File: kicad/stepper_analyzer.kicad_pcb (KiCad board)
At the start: 2 copper layers, 102 x 57 mm, 24 parts, among them J1 Connector_Conn_01x04_Male, J2 Connector_Conn_01x04_Male, M1 Motor, Q1 AO3400A, U1 ACS70331EOLCTR-2P5B3, U2 ACS70331EOLCTR-2P5B3, U3 Pico

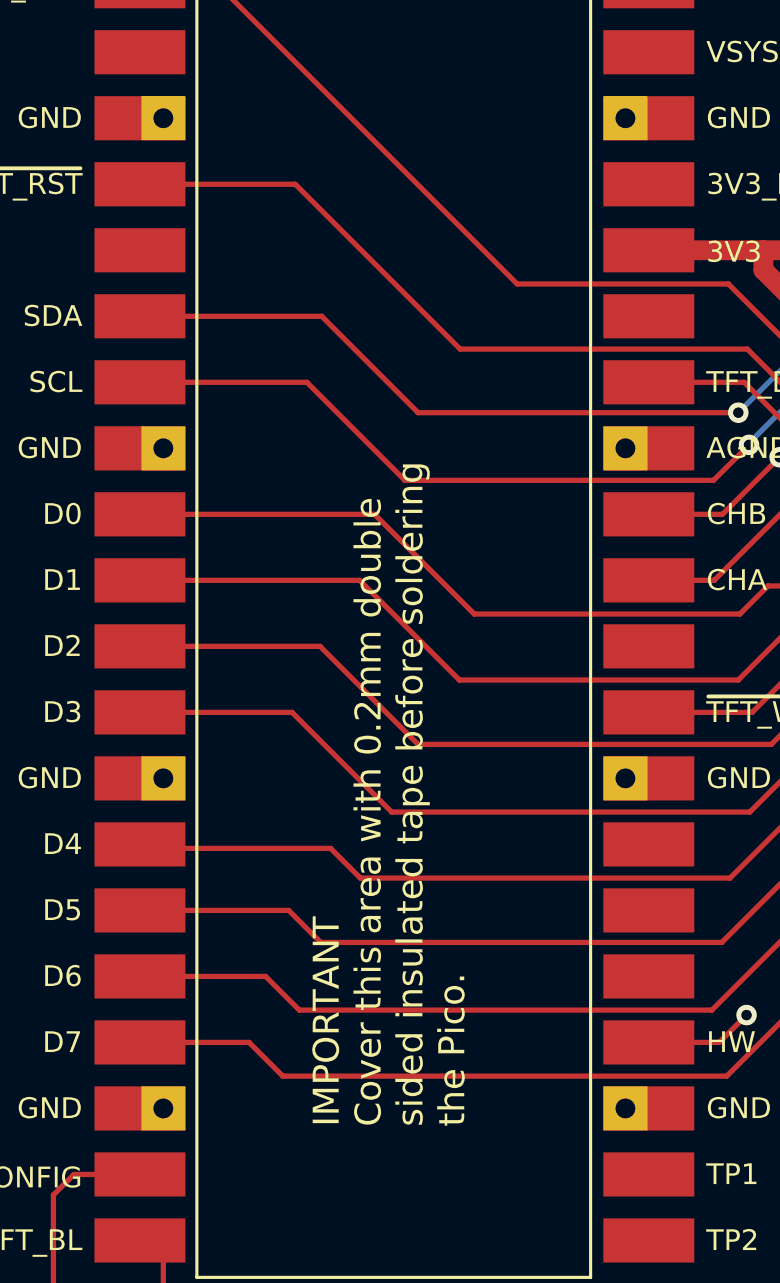
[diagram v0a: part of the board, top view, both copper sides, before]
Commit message: Updated top silk text.
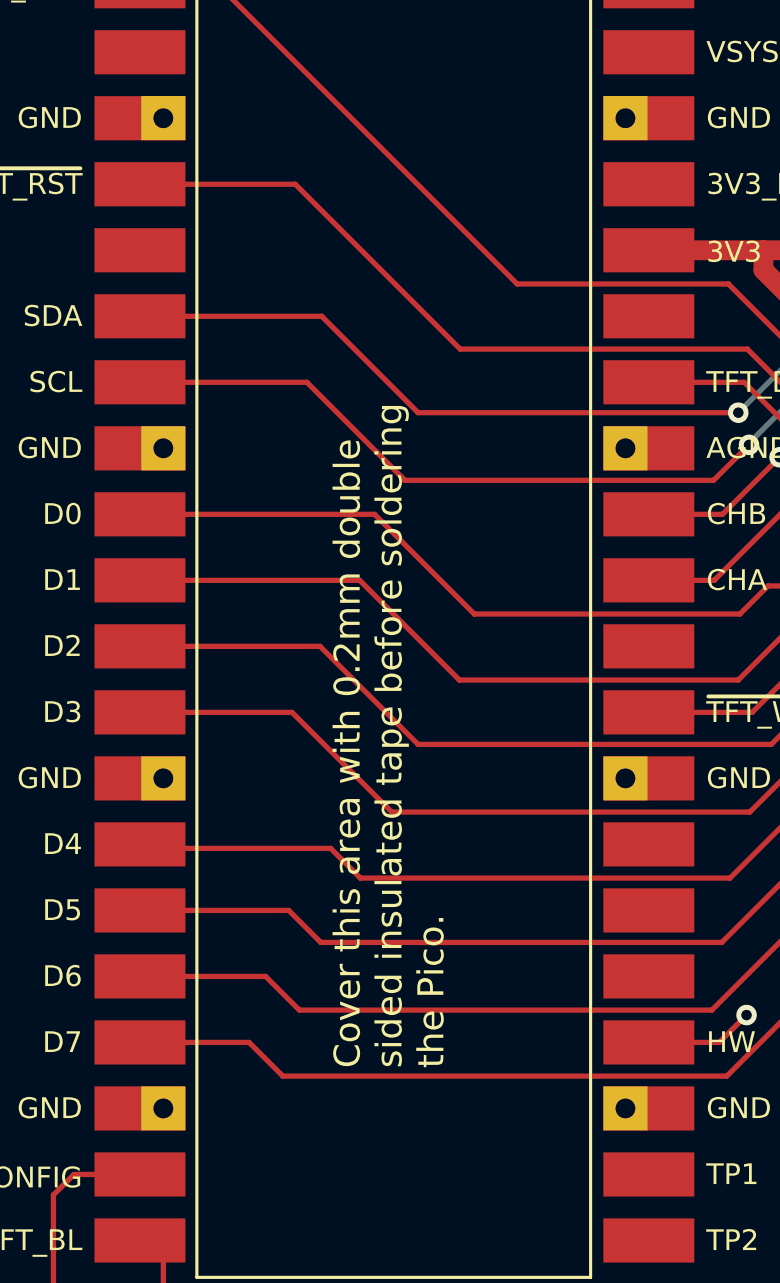
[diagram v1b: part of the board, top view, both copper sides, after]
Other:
- board text added: "Cover this area with 0.2mm double sided insulated tape before soldering the Pico."
- board text removed: "IMPORTANT Cover this area with 0.2mm double sided insulated tape before soldering the Pico."
